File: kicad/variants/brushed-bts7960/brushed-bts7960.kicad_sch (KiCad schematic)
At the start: 69 parts, among them IC1 rp2040_RP2040_breakout_swd, J1 HDR-M-2.54_1x3, J2 HDR-M-2.54_1x4, J3 HDR-M-2.54_1x4, J4 HDR-M-2.54_1x4, U1 SN74AHC244DW, U2 BTN7970, U3 BTN7970, U4 BTN7970, U5 BTN7970, U6 BMI160, U7 SPX3819M5-L-3-3/TR

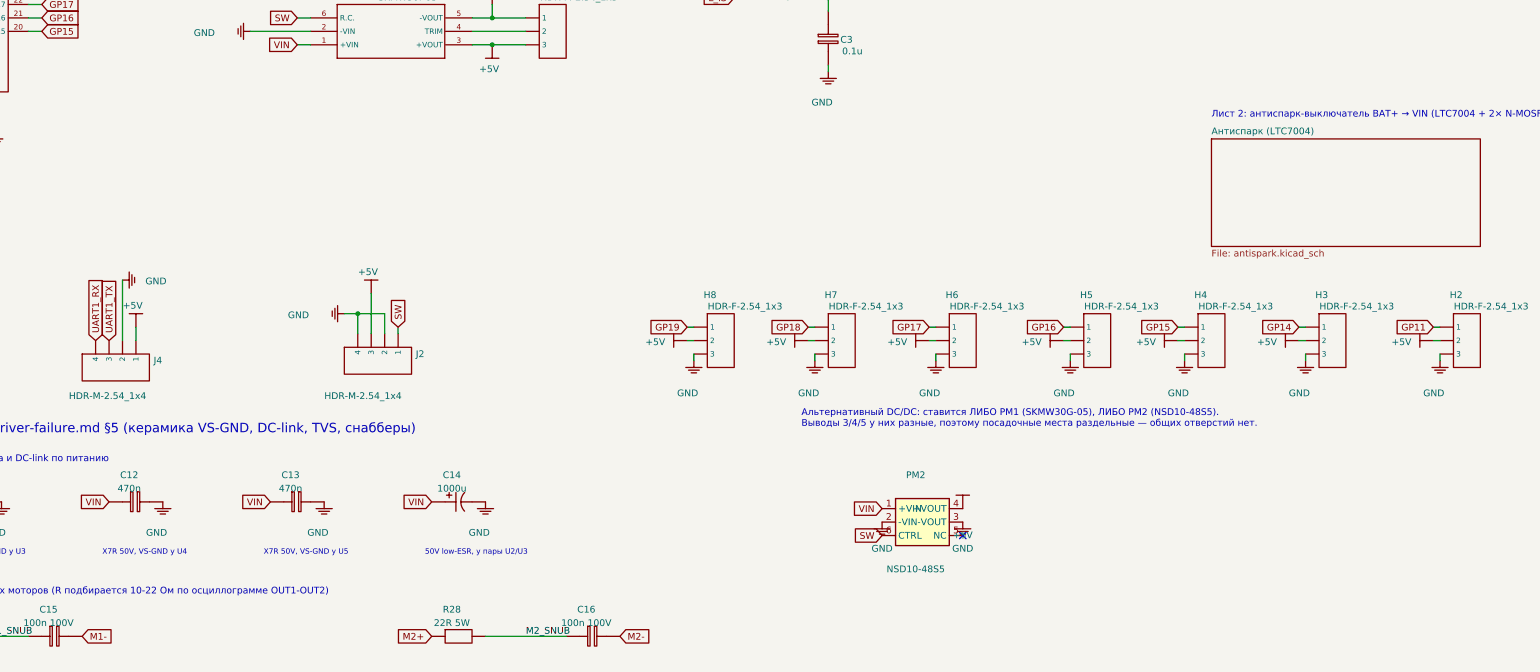
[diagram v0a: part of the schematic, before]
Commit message: feat(kicad): измерение тока/напряжения шины и единый выключатель питания (лист 2)
- antispark.kicad_sch: шунт R37 0.5 мОм + INA240A2 (U10) → IBAT, делитель 1:11 → VBAT
- перемычки JP1/JP2 для отключения датчиков с платы в пользу внешнего модуля через H10
- входы U10 разведены Kelvin-дорожками от площадок шунта
- заменён NSD10-48S5 (22–72 В) на NSD10-12S5 (9.8–36 В) — работа на разряженной 6S
- выключатель питания один: J5 (лист 2), вывод SW разъёма J2 отключён (no_connect)
- сервисная перемычка JP3 на цепи SW (R.C./CTRL DC/DC), по умолчанию открыта
- README: обзор найденных решений по счётчику коммутационных пульсаций
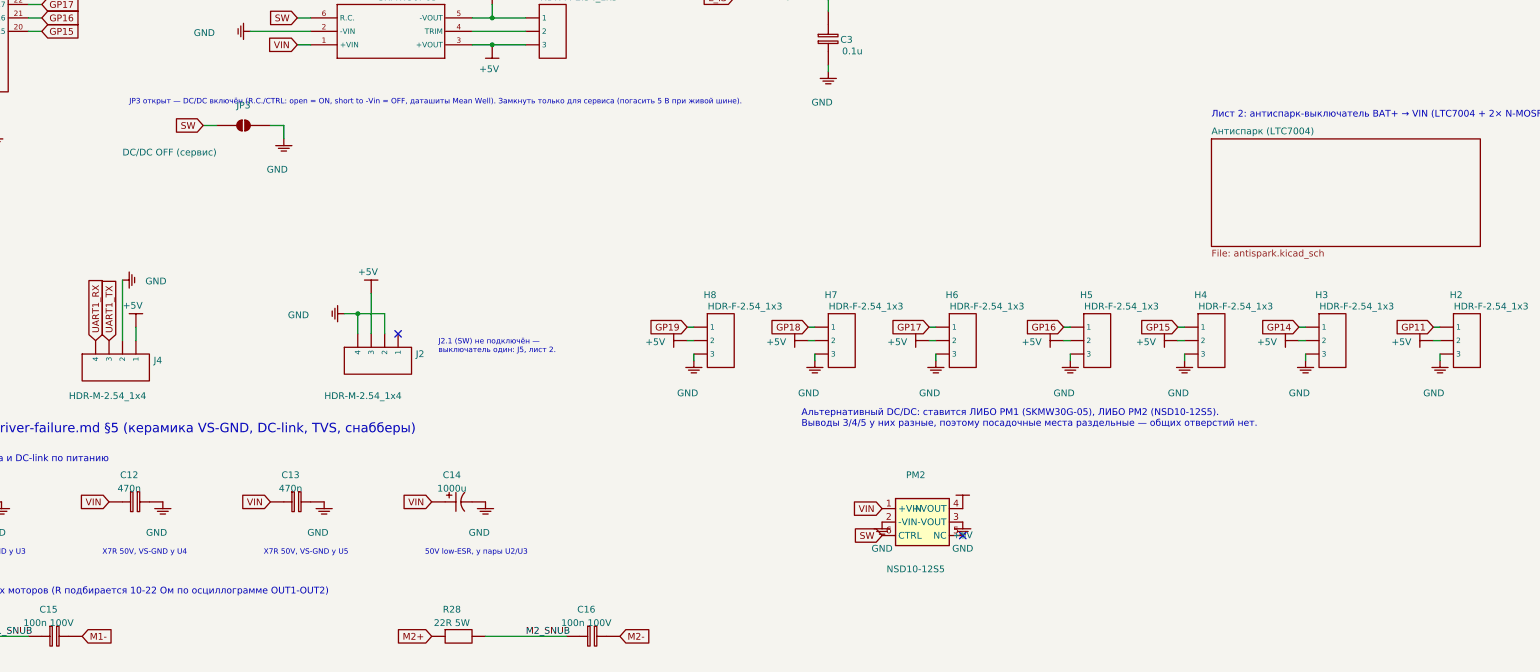
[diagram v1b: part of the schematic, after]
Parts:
- added JP3: DC/DC OFF (сервис), Jumper:SolderJumper-2_P1.3mm_Open_RoundedPad1.0x1.5mm, symbol Jumper:SolderJumper_2_Open
- PM2: value NSD10-48S5 -> NSD10-12S5; MPN NSD10-48S5 -> NSD10-12S5
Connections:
- net GND: now also JP3.2 (B)
- net SW: now also JP3.1 (A); no longer J2.1
- no-connect marks 14 -> 15
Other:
- note added: "J2.1 (SW) не подключён — выключатель один: J5, лист 2."
- note added: "JP3 открыт — DC/DC включён (R.C./CTRL: open = ON, short to -Vin = OFF, даташиты Mean Well). Замкнуть только для сервиса (погасить 5 В при живой шине)."
- note added: "Альтернативный DC/DC: ставится ЛИБО PM1 (SKMW30G-05), ЛИБО PM2 (NSD10-12S5). Выводы 3/4/5 у них разные, поэтому посадочные места раздельные — общих отверстий нет."
- note removed: "Альтернативный DC/DC: ставится ЛИБО PM1 (SKMW30G-05), ЛИБО PM2 (NSD10-48S5). Выводы 3/4/5 у них разные, поэтому посадочные места раздельные — общих отверстий нет."
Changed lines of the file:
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@@
     (instances (project "brushed-bts7960" (path "/5d1025ef-bd26-5426-bb12-5355817dfc1c" (reference "#PWR026") (unit 1))))
-  )
-  (global_label "SW" (shape input) (at 151.13 208.28 90)
-    (fields_autoplaced yes)
-    (effects (font (size 1.27 1.27)) (justify left))
-    (property "Intersheetrefs" "${INTERSHEET_REFS}" (at 151.13 208.28 0)
-      (effects (font (size 1.27 1.27)) hide))
   )
   (symbol (lib_id "biba:GND") (at 140.97 205.74 270) (unit 1)
@@
 )
   (wire (pts (xy 165.1 152.4) (xy 175.26 152.4))
-    (stroke (width 0) (type default))
-)
-  (wire (pts (xy 151.13 208.28) (xy 151.13 209.55))
     (stroke (width 0) (type default))
 )
@@
       (effects (font (size 1.27 1.27)) hide))
   )
-  (text "Альтернативный DC/DC: ставится ЛИБО PM1 (SKMW30G-05), ЛИБО PM2 (NSD10-48S5).\nВыводы 3/4/5 у них разные, поэтому посадочные места раздельные — общих отверстий нет."
+  (text "Альтернативный DC/DC: ставится ЛИБО PM1 (SKMW30G-05), ЛИБО PM2 (NSD10-12S5).\nВыводы 3/4/5 у них разные, поэтому посадочные места раздельные — общих отверстий нет."
     (at 227.33 227.33 0)
     (effects (font (size 1.27 1.27)) (justify left bottom))
@@
     (property "Reference" "PM2" (at 248.92 236.22 0)
       (effects (font (size 1.27 1.27))))
-    (property "Value" "NSD10-48S5" (at 248.92 254.00 0)
+    (property "Value" "NSD10-12S5" (at 248.92 254.00 0)
       (effects (font (size 1.27 1.27))))
     (property "Footprint" "Converter_DCDC:Converter_DCDC_MeanWell_NSD10_THT" (at 250.19 245.11 0)
@@
     (property "Package" "" (at 250.19 245.11 0) (effects (font (size 1.27 1.27)) hide))
     (property "LCSC" "" (at 250.19 245.11 0) (effects (font (size 1.27 1.27)) hide))
-    (property "MPN" "NSD10-48S5" (at 250.19 245.11 0) (effects (font (size 1.27 1.27)) hide))
+    (property "MPN" "NSD10-12S5" (at 250.19 245.11 0) (effects (font (size 1.27 1.27)) hide))
     (pin "1")
     (pin "2")
@@
         (path "/5d1025ef-bd26-5426-bb12-5355817dfc1c"
           (page "2")))))
+  (no_connect
+    (at 151.13 209.55)
+)
+  (text "J2.1 (SW) не подключён —\nвыключатель один: J5, лист 2."
+    (at 158.75 213.36 0)
+    (effects
+      (font
+        (size 1.016 1.016))
+      (justify left bottom))
+)
+  (text "JP3 открыт — DC/DC включён (R.C./CTRL: open = ON, short to -Vin = OFF, даташиты Mean Well). Замкнуть только для сервиса (погасить 5 В при живой шине)."
+    (at 100.33 166.37 0)
+    (effects
+      (font
+        (size 1.016 1.016))
+      (justify left bottom))
+)
+  (global_label "SW"
+    (shape input)
+    (at 114.3 170.18 180)
+    (fields_autoplaced yes)
+    (effects
+      (font
+        (size 1.27 1.27))
+      (justify right))
+    (property "Intersheetrefs" "${INTERSHEET_REFS}"
+      (at 114.3 170.18 0)
+      (effects
+        (font
+          (size 1.27 1.27))
+        hide)))
+  (wire
+    (pts
+      (xy 114.3 170.18)
+      (xy 116.84 170.18))
+    (stroke
+      (width 0)
+      (type default))
+)
+  (symbol
+    (lib_id "Jumper:SolderJumper_2_Open")
+    (at 121.92 170.18 0)
+    (unit 1)
+    (exclude_from_sim no)
+    (in_bom yes)
+    (on_board yes)
+    (dnp no)
+    (property "Reference" "JP3"
+      (at 121.92 166.37 0)
+      (effects
+        (font
+          (size 1.27 1.27))))
+    (property "Value" "DC/DC OFF (сервис)"
+      (at 107.95 175.26 0)
+      (effects
+        (font
+          (size 1.27 1.27))))
+    (property "Footprint" "Jumper:SolderJumper-2_P1.3mm_Open_RoundedPad1.0x1.5mm"
+      (at 121.92 170.18 0)
+      (effects
+        (font
+          (size 1.27 1.27))
+        hide))
+    (property "Datasheet" ""
+      (at 121.92 170.18 0)
+      (effects
+        (font
+          (size 1.27 1.27))
+        hide))
+    (property "Package" ""
+      (at 121.92 170.18 0)
+      (effects
+        (font
+          (size 1.27 1.27))
+        hide))
+    (property "LCSC" ""
+      (at 121.92 170.18 0)
+      (effects
+        (font
+          (size 1.27 1.27))
+        hide))
+    (property "MPN" ""
+      (at 121.92 170.18 0)
+      (effects
+        (font
+          (size 1.27 1.27))
+        hide))
+    (pin "1"
+)
+    (pin "2"
+)
+    (instances
+      (project "brushed-bts7960"
+        (path "/5d1025ef-bd26-5426-bb12-5355817dfc1c"
+          (reference "JP3")
+          (unit 1)))))
+  (wire
+    (pts
+      (xy 127.0 170.18)
+      (xy 129.54 170.18))
+    (stroke
+      (width 0)
+      (type default))
+)
+  (wire
+    (pts
+      (xy 129.54 170.18)
+      (xy 129.54 172.72))
+    (stroke
+      (width 0)
+      (type default))
+)
+  (symbol
+    (lib_id "biba:GND")
+    (at 129.54 172.72 0)
+    (unit 1)
+    (exclude_from_sim no)
+    (in_bom no)
+    (on_board no)
+    (dnp no)
+    (property "Reference" "#PWR123"
+      (at 129.54 172.72 0)
+      (effects
+        (font
+          (size 1.27 1.27))
+        hide))
+    (property "Value" "GND"
+      (at 128.3 178.5 0)
+      (effects
+        (font
+          (size 1.27 1.27))))
+    (property "Footprint" ""
+      (at 129.54 172.72 0)
+      (effects
+        (font
+          (size 1.27 1.27))
+        hide))
+    (property "Datasheet" ""
+      (at 129.54 172.72 0)
+      (effects
+        (font
+          (size 1.27 1.27))
+        hide))
+    (pin "1"
+)
+    (instances
+      (project "brushed-bts7960"
+        (path "/5d1025ef-bd26-5426-bb12-5355817dfc1c"
+          (reference "#PWR123")
+          (unit 1)))))
   (sheet_instances
     (path "/" (page "1"))

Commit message: feat(kicad): интерфейс дочерней платы счётчика пульсаций (лист 3, J6 + JP4/JP5)
Основная плата даёт только разъём J6 (1×14) и паяльные перемычки JP4/JP5
в разрыве L_IS/R_IS → ADC_L/ADC_R. Обработка пульсаций живёт на сменной
дочерней плате, впаиваемой перпендикулярно; первая версия — LM2917.

- ripple.kicad_sch: лист 3 с J6, JP4/JP5 и метками L_IS/R_IS, ADC_L/ADC_R
- brushed-bts7960.kicad_sch: IC1.31/32 переименованы R_IS/L_IS → ADC_R/ADC_L,
  добавлен иерархический лист, поправлен текст листа 2
- brushed-bts7960.kicad_pro: лист «Счётчик пульсаций (интерфейс)» в sheets
- target.h/target.md: GP10/GP11 и GP16–GP19 помечены как зарезервированные
  под J6, GP26/GP27 заведены через JP5/JP4
- README.md: таблица J6, схема врезки перемычек и бриф дочерней платы
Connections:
- net L_IS: no longer IC1.32 (GP27)
- net R_IS: no longer IC1.31 (GP26)
- new net ADC_L: IC1.32 (GP27)
- new net ADC_R: IC1.31 (GP26)
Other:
- added sheet Счётчик пульсаций (интерфейс) (ripple.kicad_sch)
- note added: "Лист 2: антиспарк BAT+ → VIN (LTC7004, 2× MOSFET, выключатель J5), измерение шины (шунт + INA240 → IBAT, делитель → VBAT)."
- note added: "Лист 3 (справа): J6 дочерней платы счётчика пульсаций, JP4/JP5 в разрыве L_IS/R_IS → ADC_L/ADC_R (IC1.32/31)."
- note removed: "Лист 2: антиспарк-выключатель BAT+ → VIN (LTC7004 + 2× N-MOSFET, мягкий старт RC, выключатель J5). Клемма батареи на плате становится BAT+, VIN — шина после ключа."
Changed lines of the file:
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@@
       (effects (font (size 1.27 1.27)) hide))
   )
-  (global_label "L_IS" (shape input) (at 83.82 127 0)
+  (global_label "ADC_L" (shape input) (at 83.82 127 0)
     (fields_autoplaced yes)
     (effects (font (size 1.27 1.27)) (justify left))
@@
       (effects (font (size 1.27 1.27)) hide))
   )
-  (global_label "R_IS" (shape input) (at 83.82 129.54 0)
+  (global_label "ADC_R" (shape input) (at 83.82 129.54 0)
     (fields_autoplaced yes)
     (effects (font (size 1.27 1.27)) (justify left))
@@
   )
   (no_connect (at 257.81 247.65))
-  (text "Лист 2: антиспарк-выключатель BAT+ → VIN (LTC7004 + 2× N-MOSFET, мягкий старт RC, выключатель J5). Клемма батареи на плате становится BAT+, VIN — шина после ключа."
+  (text "Лист 2: антиспарк BAT+ → VIN (LTC7004, 2× MOSFET, выключатель J5),\nизмерение шины (шунт + INA240 → IBAT, делитель → VBAT)."
     (at 304.8 168.91 0)
     (effects
       (font
-        (size 1.27 1.27))
+        (size 1.016 1.016))
       (justify left bottom))
 )
   (sheet
     (at 304.8 172.72)
-    (size 50.8 20.32)
+    (size 45.72 20.32)
     (fields_autoplaced yes)
     (stroke
@@
           (reference "#PWR123")
           (unit 1)))))
+  (text "Лист 3 (справа): J6 дочерней платы счётчика пульсаций,\nJP4/JP5 в разрыве L_IS/R_IS → ADC_L/ADC_R (IC1.32/31)."
+    (at 304.8 162.56 0)
+    (effects
+      (font
+        (size 1.016 1.016))
+      (justify left bottom))
+)
+  (sheet
+    (at 353.06 172.72)
+    (size 45.72 20.32)
+    (fields_autoplaced yes)
+    (stroke
+      (width 0.1524)
+      (type solid))
+    (fill
+      (color 0 0 0 0.0000))
+    (property "Sheetname" "Счётчик пульсаций (интерфейс)"
+      (at 353.06 172.0 0)
+      (effects
+        (font
+          (size 1.27 1.27))
+        (justify left bottom)))
+    (property "Sheetfile" "ripple.kicad_sch"
+      (at 353.06 193.6 0)
+      (effects
+        (font
+          (size 1.27 1.27))
+        (justify left top)))
+    (instances
+      (project "brushed-bts7960"
+        (path "/5d1025ef-bd26-5426-bb12-5355817dfc1c"
+          (page "3")))))
   (sheet_instances
     (path "/" (page "1"))
